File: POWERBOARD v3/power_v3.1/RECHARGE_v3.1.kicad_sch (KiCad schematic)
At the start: 27 parts, among them J1 B2B_PH_K_S, J2 USB_C_Receptacle_USB2.0_16P, J3 R14 - 103AT-2, U1 USBLC6-2, U2 BQ25886RGE

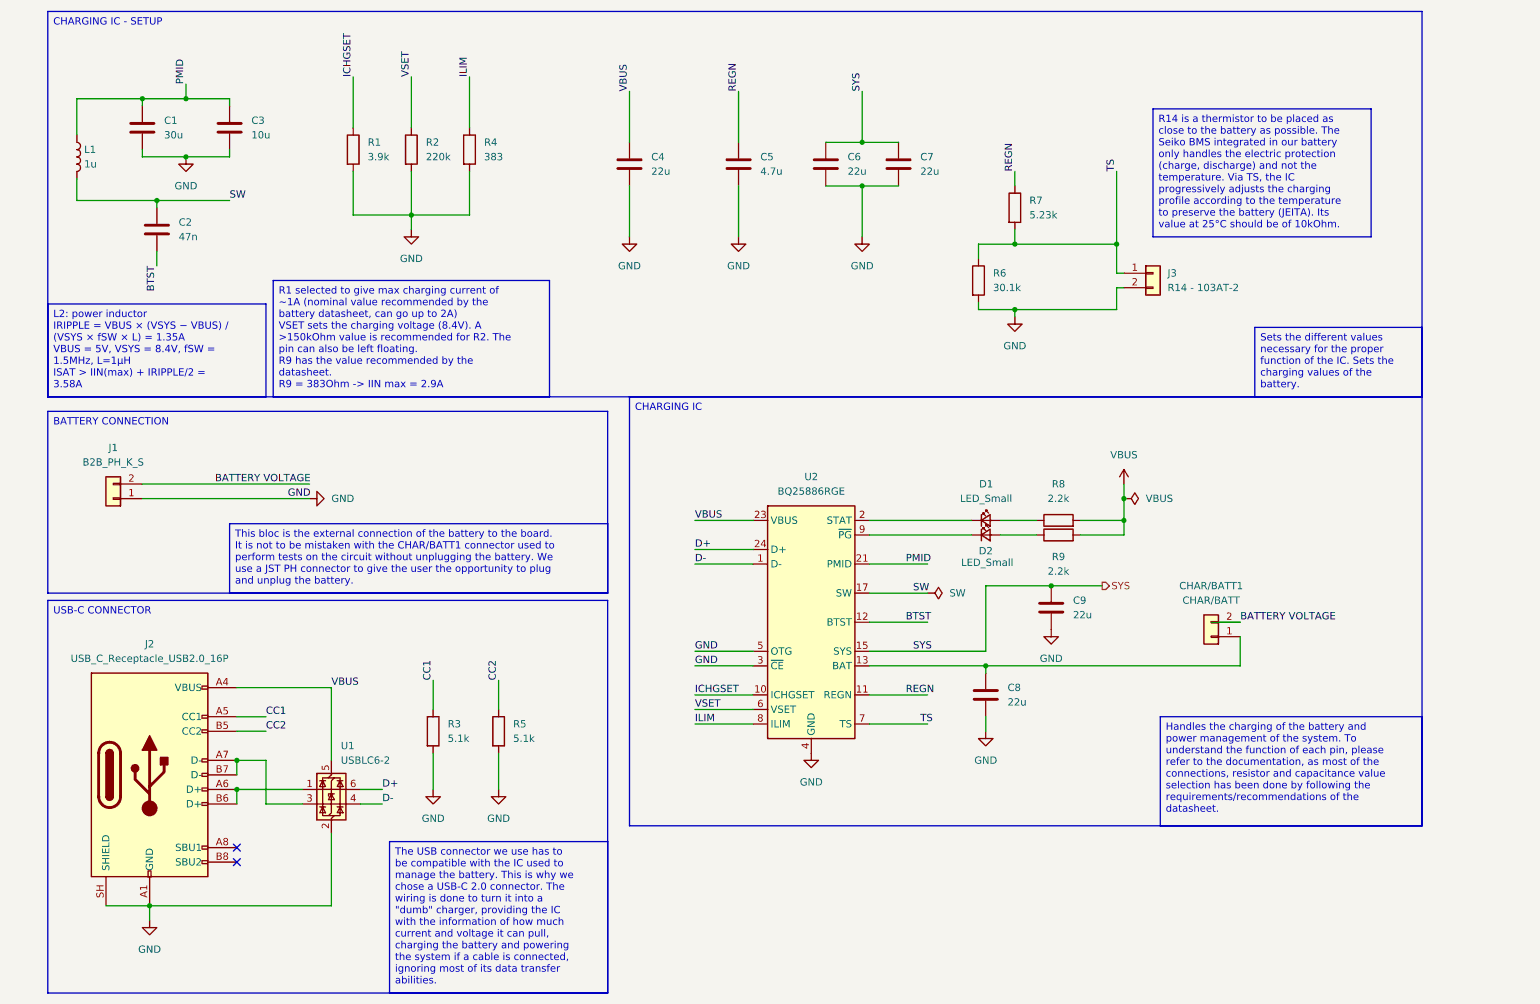
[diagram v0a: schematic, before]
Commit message: Added a comparator circuit that disables the buck converter when temp is too high and re enables it when it reaches a lower temperature
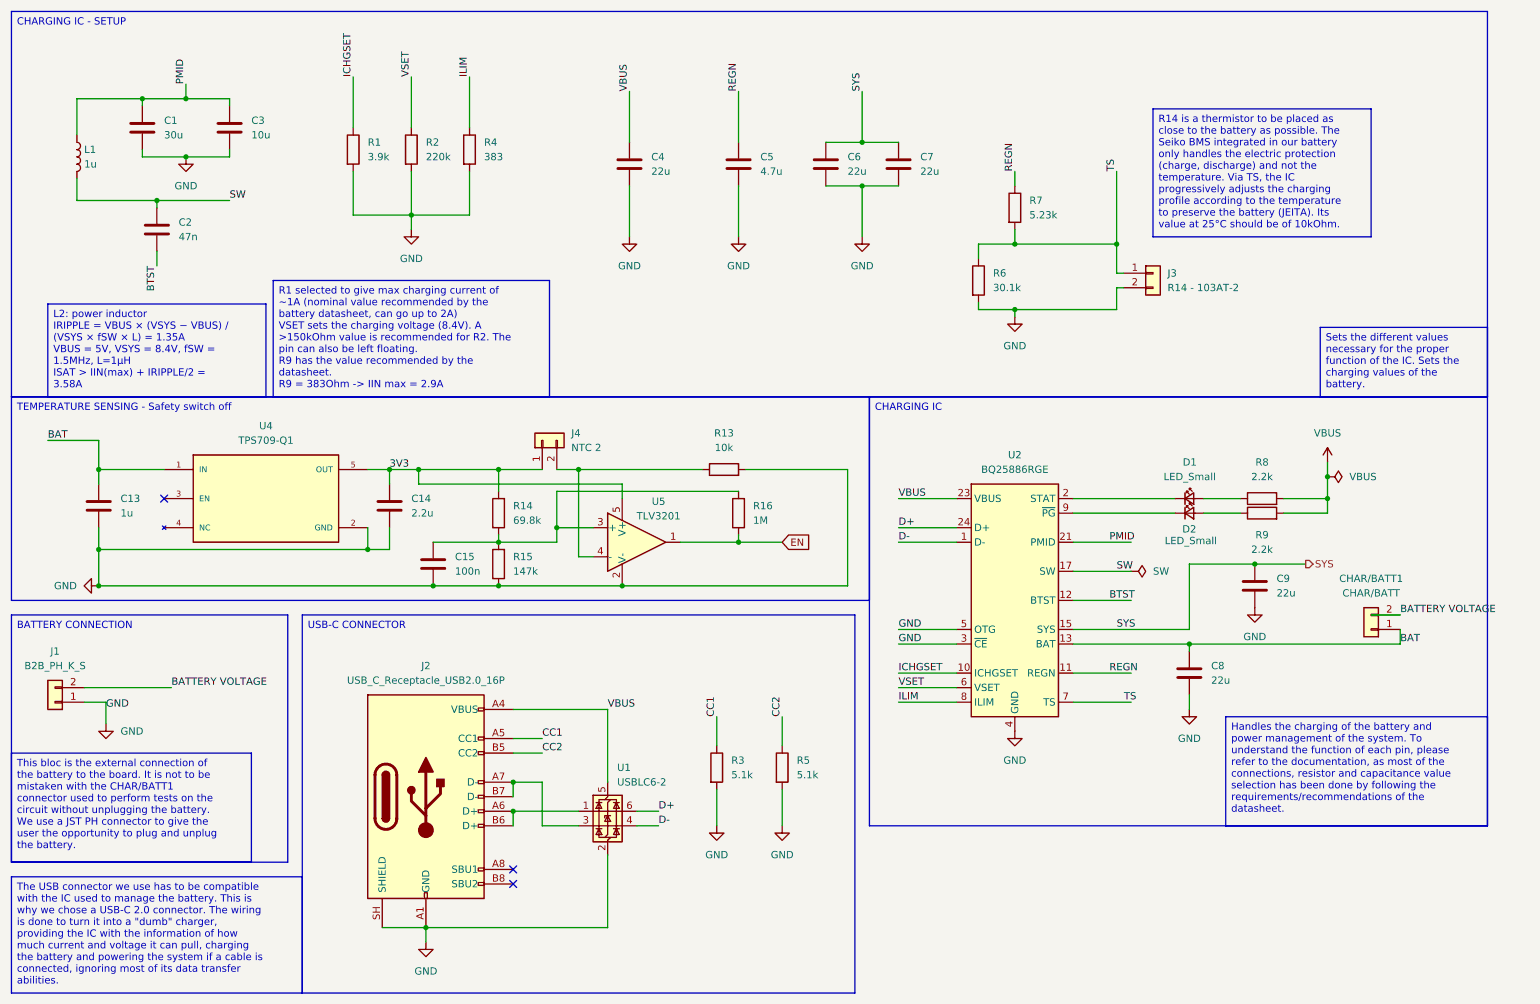
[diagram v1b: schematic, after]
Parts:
- added C13: 1u, symbol Device:C
- added C14: 2.2u, symbol Device:C
- added C15: 100n, symbol Device:C
- added J4: NTC 2, symbol Connector_Generic:Conn_01x02
- added R13: 10k, symbol Device:R
- added R14: 69.8k, symbol Device:R
- added R15: 147k, symbol Device:R
- added R16: 1M, symbol Device:R
- added U4: TPS709-Q1, TPS70933DBVR:SOT95P280X145-5N, symbol Custom:TPS70933DBVR
- added U5: TLV3201, Package_TO_SOT_SMD:SOT-23-5, symbol Amplifier_Operational:TLV365DBV
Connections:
- net GND: now also C13.2, C14.2, C15.2, R13.2, R15.1, U4.2 (GND), U5.2 (V-)
- net BAT: now reaches C8.1, CHAR/BATT1.1 (Pin_1), U2.13 (BAT), U2.14 (BAT)
- net BAT: now also C13.1, U4.1 (IN)
- new net: C15.1, R14.1, R15.2, R16.2, U5.3 (+)
- new net: J4.2 (Pin_2), R13.1, U5.4 (-)
- new net 3V3: C14.1, J4.1 (Pin_1), R14.2, U4.5 (OUT), U5.5 (V+)
- new net EN: R16.1, U5.1
- no-connect marks 2 -> 3
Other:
- moved on the sheet: C8, C9, CHAR/BATT1, D1, D2, J1, J2, R3, R5, R8, R9, U1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

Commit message: Final changes before v3.2
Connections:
- net 3V3: no longer names the net of C14.1, J4.1 (Pin_1), R14.2, U4.5 (OUT), U5.5 (V+)
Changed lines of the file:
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@@
-		)
-	)
-	(label "3V3"
-		(at 87.63 101.6 0)
-		(effects
-			(font
-				(size 1.27 1.27)
-			)
-			(justify left bottom)
 		)
 	)
